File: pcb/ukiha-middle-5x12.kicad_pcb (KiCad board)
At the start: 2 copper layers, 100 x 111.5 mm, 12 parts

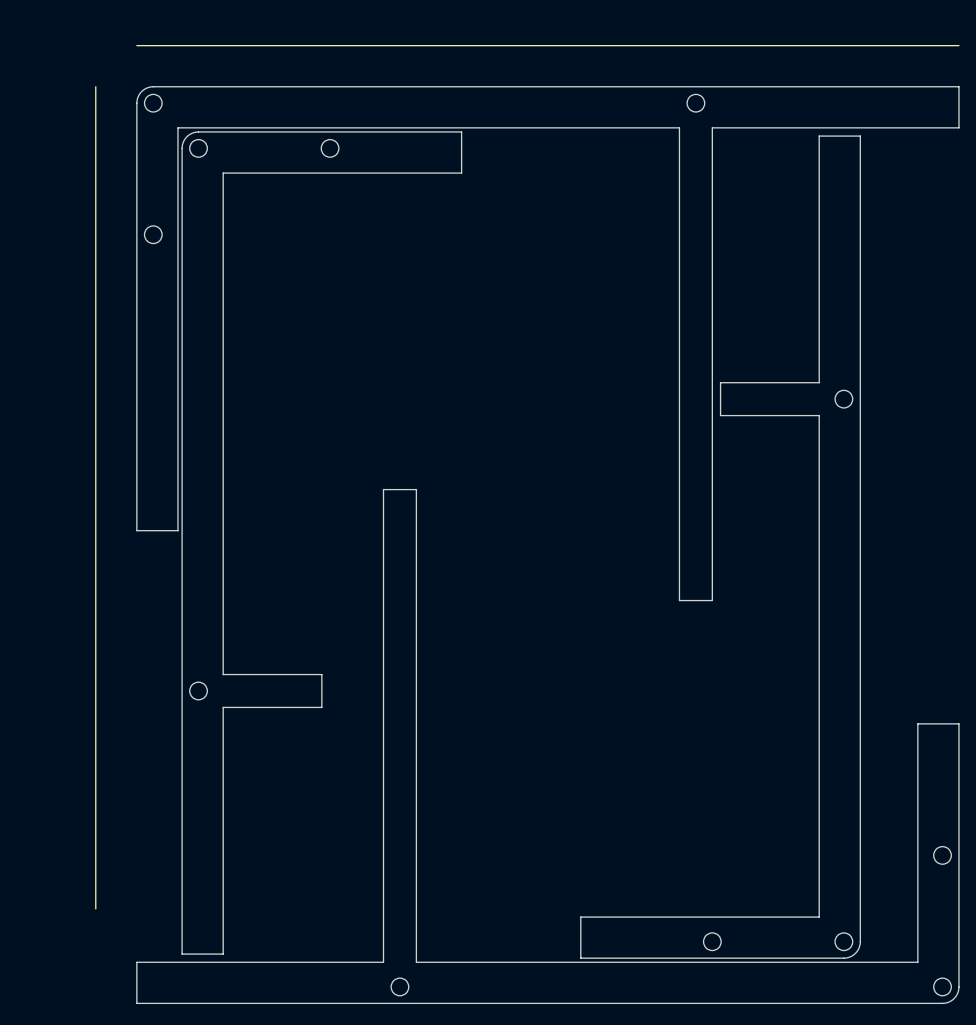
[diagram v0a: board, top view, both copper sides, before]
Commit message: Add 48 key middle plate
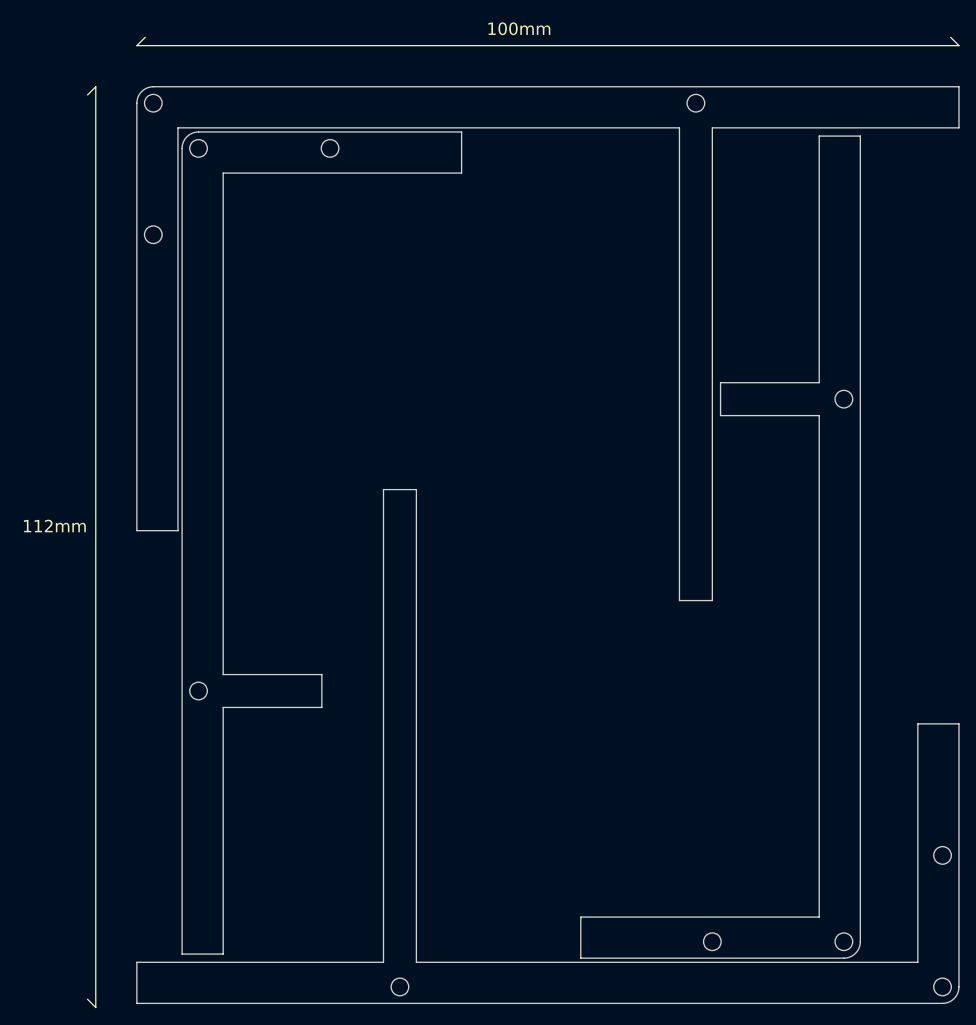
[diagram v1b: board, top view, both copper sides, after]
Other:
- board text added: "100mm"
- board text added: "112mm"
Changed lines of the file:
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@@
   (general
     (thickness 1.6)
-    (drawings 46)
+    (drawings 52)
     (tracks 0)
     (zones 0)
@@
     (pad_to_mask_clearance 0.2)
     (solder_mask_min_width 0.25)
-    (aux_axis_origin 37.70322 52.784508)
+    (aux_axis_origin 27.102501 36.80625)
     (grid_origin 27.102501 36.80625)
     (visible_elements 7FFFFFEF)
@@
       (padsonsilk false)
       (subtractmaskfromsilk true)
-      (outputformat 1)
+      (outputformat 5)
       (mirror false)
       (drillshape 0)
@@
     (fp_circle (center 0 0) (end 1.07 0) (layer Edge.Cuts) (width 0.15))
   )
+  (gr_text 112mm (at 17.102501 90.30625) (layer F.SilkS)
+    (effects (font (size 1.5 1.5) (thickness 0.3)))
+  )
+  (gr_line (start 22.102501 36.80625) (end 21.102501 37.80625) (layer F.SilkS) (width 0.15))
+  (gr_line (start 22.102501 148.80625) (end 21.102501 147.80625) (layer F.SilkS) (width 0.15))
+  (gr_text 100mm (at 73.602501 29.80625) (layer F.SilkS)
+    (effects (font (size 1.5 1.5) (thickness 0.3)))
+  )
+  (gr_line (start 127.102501 31.80625) (end 126.102501 30.80625) (layer F.SilkS) (width 0.15))
+  (gr_line (start 27.102501 31.80625) (end 28.102501 30.80625) (layer F.SilkS) (width 0.15))
   (gr_line (start 110.102501 72.80625) (end 110.102501 42.80625) (layer Edge.Cuts) (width 0.15))
   (gr_line (start 98.102501 76.80625) (end 98.102501 72.80625) (layer Edge.Cuts) (width 0.15))
@@
   (gr_line (start 97.102501 99.30625) (end 93.102501 99.30625) (layer Edge.Cuts) (width 0.15))
   (gr_arc (start 29.102501 38.80625) (end 29.102501 36.80625) (angle -90) (layer Edge.Cuts) (width 0.15))
-  (gr_line (start 22.102501 36.80625) (end 22.102501 136.80625) (layer F.SilkS) (width 0.15))
+  (gr_line (start 22.102501 36.80625) (end 22.102501 148.80625) (layer F.SilkS) (width 0.15))
   (gr_line (start 27.102501 31.80625) (end 127.102501 31.80625) (layer F.SilkS) (width 0.15))
 )

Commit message: Fix screw hole position
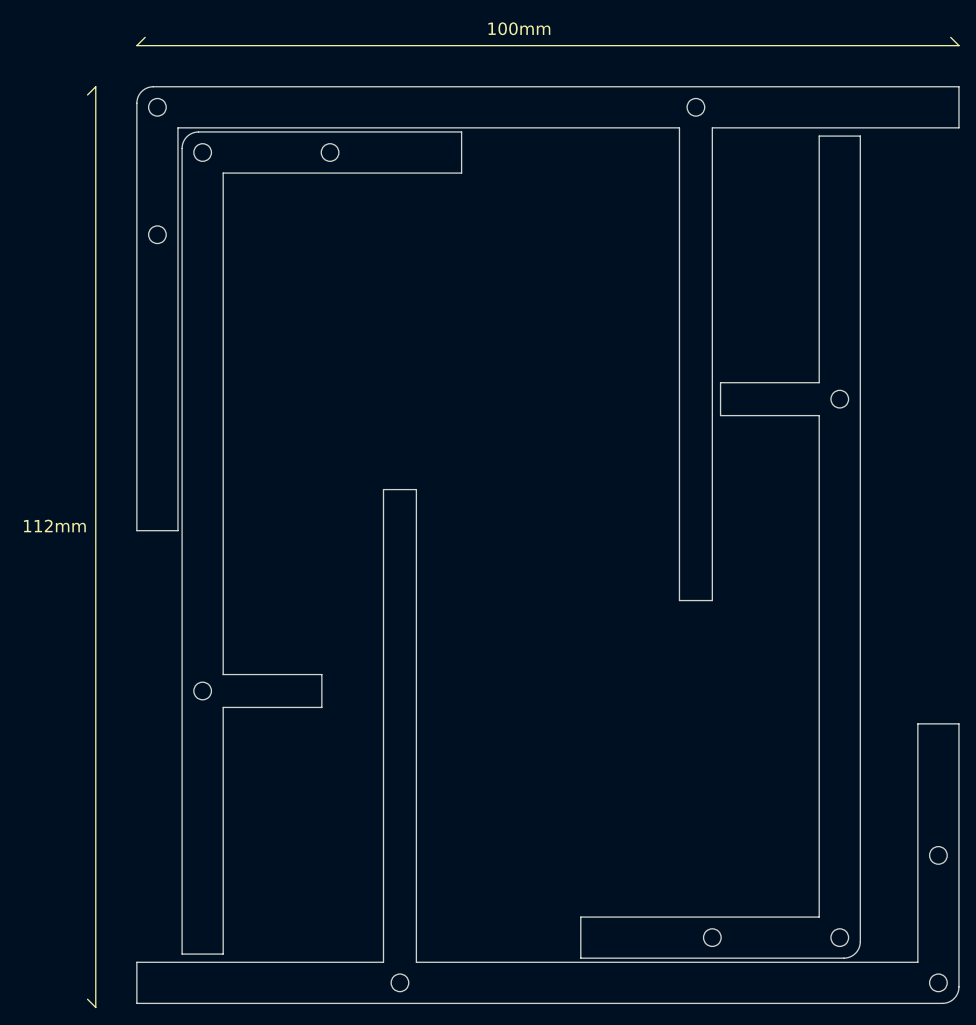
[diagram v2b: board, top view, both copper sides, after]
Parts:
- moved ? 0.71 mm to (29.6, 39.3)
- moved ? 0.71 mm to (112.6, 140.3)
- moved ? 0.71 mm to (35.1, 44.8)
- moved ? 0.71 mm to (124.6, 145.8)
- moved ? 0.50 mm to (112.6, 74.8)
- moved ? 0.50 mm to (29.6, 54.8)
- moved ? 0.50 mm to (95.1, 39.3)
- moved ? 0.50 mm to (97.1, 140.3)
- moved ? 0.50 mm to (50.6, 44.8)
- moved ? 0.50 mm to (35.1, 110.3)
- moved ? 0.50 mm to (124.6, 130.3)
- moved ? 0.50 mm to (59.1, 145.8)
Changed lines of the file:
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@@
     (visible_elements 7FFFFFEF)
     (pcbplotparams
-      (layerselection 0x010f0_ffffffff)
+      (layerselection 0x01000_7ffffffe)
       (usegerberextensions false)
       (usegerberattributes false)
@@
   )
   (module "#footprint:M2_Hole_Edge.Cuts" (layer F.Cu)
-    (at 113.102501 74.80625 90)
+    (at 112.602501 74.80625 90)
     (descr "Resitance 3 pas")
     (tags R)
@@
   )
   (module "#footprint:M2_Hole_Edge.Cuts" (layer F.Cu)
-    (at 113.102501 140.80625 90)
+    (at 112.602501 140.30625 90)
     (descr "Resitance 3 pas")
     (tags R)
@@
   )
   (module "#footprint:M2_Hole_Edge.Cuts" (layer F.Cu)
-    (at 97.102501 140.80625 90)
+    (at 97.102501 140.30625 90)
     (descr "Resitance 3 pas")
     (tags R)
@@
   )
   (module "#footprint:M2_Hole_Edge.Cuts" (layer F.Cu)
-    (at 34.602501 44.30625 270)
+    (at 35.102501 44.80625 270)
     (descr "Resitance 3 pas")
     (tags R)
@@
   )
   (module "#footprint:M2_Hole_Edge.Cuts" (layer F.Cu)
-    (at 50.602501 44.30625 270)
+    (at 50.602501 44.80625 270)
     (descr "Resitance 3 pas")
     (tags R)
@@
   )
   (module "#footprint:M2_Hole_Edge.Cuts" (layer F.Cu)
-    (at 34.602501 110.30625 270)
+    (at 35.102501 110.30625 270)
     (descr "Resitance 3 pas")
     (tags R)
@@
   )
   (module "#footprint:M2_Hole_Edge.Cuts" (layer F.Cu)
-    (at 125.102501 130.30625 180)
+    (at 124.602501 130.30625 180)
     (descr "Resitance 3 pas")
     (tags R)
@@
   )
   (module "#footprint:M2_Hole_Edge.Cuts" (layer F.Cu)
-    (at 59.102501 146.30625 180)
+    (at 59.102501 145.80625 180)
     (descr "Resitance 3 pas")
     (tags R)
@@
   )
   (module "#footprint:M2_Hole_Edge.Cuts" (layer F.Cu)
-    (at 125.102501 146.30625 180)
+    (at 124.602501 145.80625 180)
     (descr "Resitance 3 pas")
     (tags R)
@@
   )
   (module "#footprint:M2_Hole_Edge.Cuts" (layer F.Cu)
-    (at 29.102501 54.80625)
+    (at 29.602501 54.80625)
     (descr "Resitance 3 pas")
     (tags R)
@@
   )
   (module "#footprint:M2_Hole_Edge.Cuts" (layer F.Cu)
-    (at 29.102501 38.80625)
+    (at 29.602501 39.30625)
     (descr "Resitance 3 pas")
     (tags R)
@@
   )
   (module "#footprint:M2_Hole_Edge.Cuts" (layer F.Cu)
-    (at 95.102501 38.80625)
-    (descr "Resitance 3 pas")
-    (tags R)
+    (at 95.102501 39.30625)
+    (descr "Resitance 3 pas")
+    (tags R)
